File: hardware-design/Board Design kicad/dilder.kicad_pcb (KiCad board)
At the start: 4 copper layers, 45 x 80 mm, 27 parts, among them J1 USB-C, J2 BAT, J3 ePaper, Q1 FS8205A, SW1 5-Way, U1 ESP32-S3-N16R8, U2 TP4056, U3 DW01A, U4 AMS1117-3.3, U6 MPU-6050

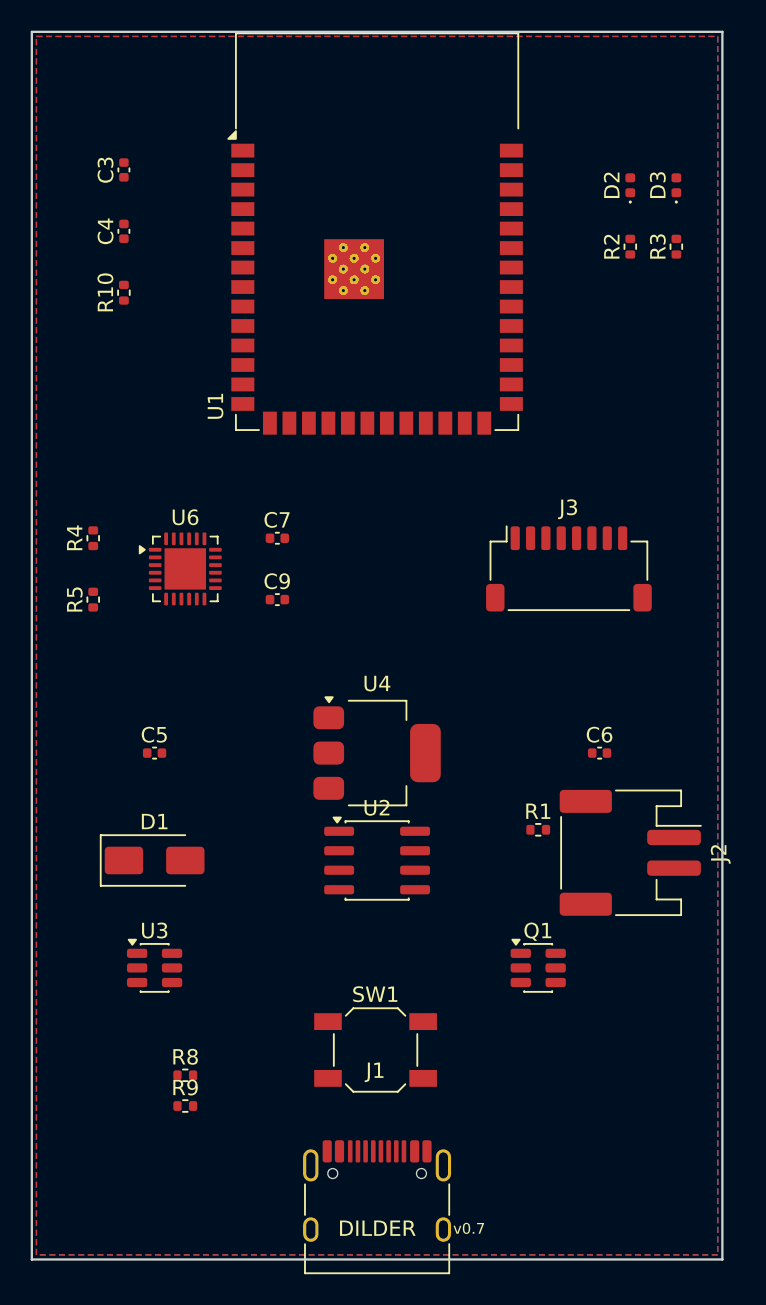
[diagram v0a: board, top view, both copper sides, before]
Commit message: Add v0.4 PCB routing, board design doc, update prompts, Prompt #155
Route the v0.4 board (30x70mm, 4-layer) with route_v04.py: B.Cu channels
for I2C/USB/joystick/ePaper, staggered L-routes for crossing-free SPI,
custom paths for EN/BOOT/battery protection, F.Cu power chain. Adds In1.Cu
GND plane and In2.Cu 3V3 plane with stitching vias. Board design doc
captures zones, BOM, GPIO map, routing strategy, and DRC status. Updates
prompts index with #154-155.

Co-Authored-By: Claude Opus 4.6 (1M context) <noreply@anthropic.com>
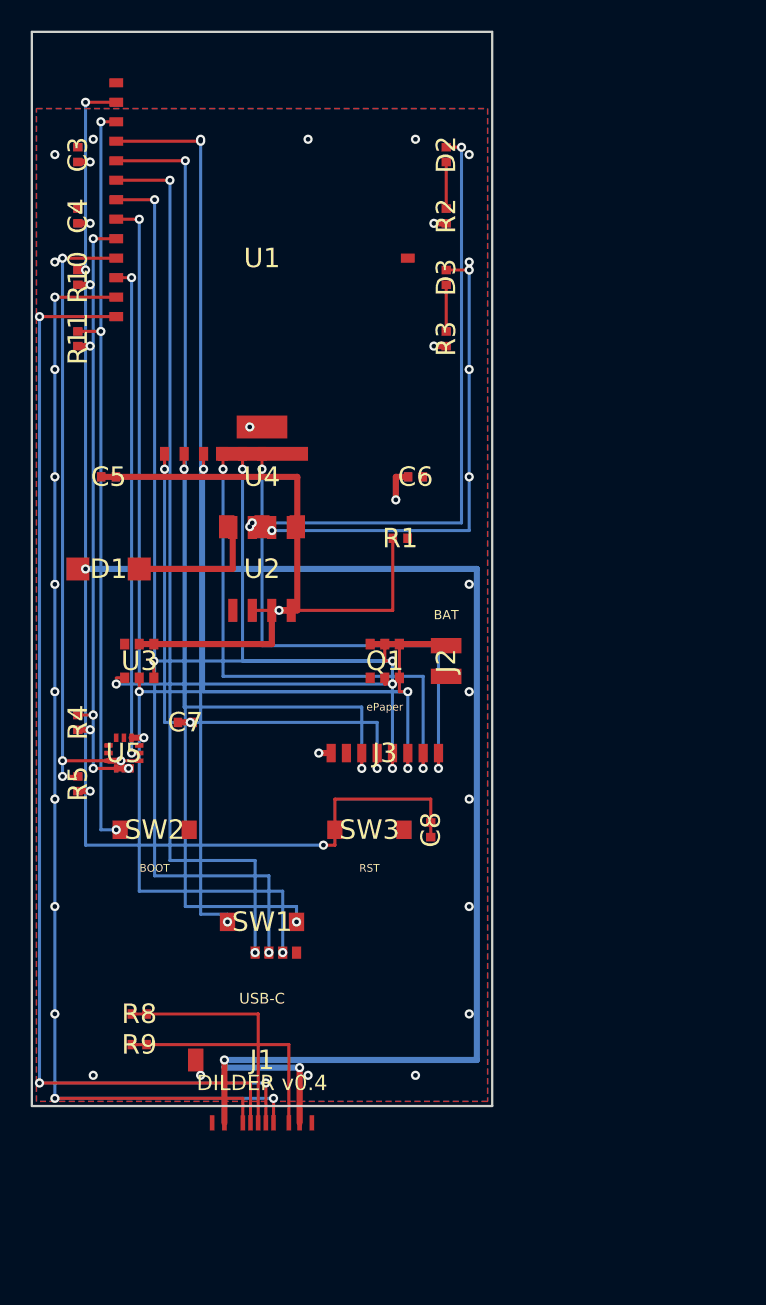
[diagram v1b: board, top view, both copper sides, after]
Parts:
- removed C9: 100nF, C_0402_1005Metric
- removed U6: MPU-6050, QFN-24-1EP_4x4mm_P0.5mm_EP2.7x2.7mm
- added C8: 100nF, , F.Cu at (126.0, 152.0)
- added R11: 10k, , F.Cu at (103.0, 120.0)
- added SW2: BOOT, , F.Cu at (108.0, 152.0)
- added SW3: RESET, , F.Cu at (122.0, 152.0)
- added U5: LIS2DH12TR, , F.Cu at (106.0, 147.0)
- C3, C4, C5, C6, C7: footprint C_0402_1005Metric -> (none)
- D1: footprint D_SMA -> (none)
- D2, D3: footprint LED_0402_1005Metric -> (none)
- J1: footprint USB_C_Receptacle_HRO_TYPE-C-31-M-12 -> (none)
- J2: footprint JST_PH_S2B-PH-SM4-TB_1x02-1MP_P2.00mm_Horizontal -> (none)
- J3: footprint JST_SH_SM08B-SRSS-TB_1x08-1MP_P1.00mm_Horizontal -> (none)
- Q1, U3: footprint SOT-23-6 -> (none)
- R1, R10, R2, R3, R4, R5, R8, R9: footprint R_0402_1005Metric -> (none)
- SW1: footprint SW_SPST_SKQG_WithStem -> (none)
- U1: footprint ESP32-S3-WROOM-1 -> (none)
- U2: footprint SOIC-8_3.9x4.9mm_P1.27mm -> (none)
- U4: footprint SOT-223-3_TabPin2 -> (none)
- moved Q1 22.4 mm to (123.0, 141.0)
- moved C6 21.6 mm to (125.0, 129.0)
- moved R1 21.0 mm to (124.0, 133.0)
- moved U2 20.4 mm to (115.0, 135.0)
- moved U3 20.0 mm to (107.0, 141.0)
- moved U4 19.5 mm to (115.0, 129.0)
- moved D1 19.2 mm to (105.0, 135.0)
- moved C5 18.2 mm to (105.0, 129.0)
- moved J2 17.3 mm to (127.0, 141.0)
- moved J3 17.0 mm to (123.0, 147.0)
- moved D3 16.2 mm to (127.0, 116.0)
- moved R3 16.2 mm to (127.0, 120.0)
- moved C7 13.4 mm to (110.0, 145.0)
- moved J1 12.5 mm to (115.0, 167.0)
- moved D2 12.2 mm to (127.0, 108.0)
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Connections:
- SW1 pad 1: GND -> JOY_UP
- SW1 pad 2: JOY_CENTER -> JOY_DOWN
- U1 pad 11: (no net) -> ACCEL_INT1
- U1 pad 27: (no net) -> BOOT
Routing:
- net USB_DP: track 0.00 -> 88.6 mm, vias 0 -> 3
- net VBUS: track 0.00 -> 87.5 mm, vias 0 -> 3
- net USB_DM: track 0.00 -> 85.9 mm, vias 0 -> 3
- net EN: track 0.00 -> 78.9 mm, vias 0 -> 3
- net JOY_DOWN: track 0.00 -> 61.3 mm, vias 0 -> 2
- net JOY_LEFT: track 0.00 -> 59.4 mm, vias 0 -> 2
- net JOY_RIGHT: track 0.00 -> 59.0 mm, vias 0 -> 2
- net JOY_CENTER: track 0.00 -> 58.6 mm, vias 0 -> 2
- net JOY_UP: track 0.00 -> 58.1 mm, vias 0 -> 2
- net BOOT: track 0.00 -> 50.1 mm, vias 0 -> 3
- net I2C_SCL: track 0.00 -> 43.3 mm, vias 0 -> 3
- net I2C_SDA: track 0.00 -> 39.5 mm, vias 0 -> 3
- net CHRG_OUT: track 0.00 -> 39.4 mm, vias 0 -> 2
- net EPD_CLK: track 0.00 -> 35.3 mm, vias 0 -> 2
- net EPD_DC: track 0.00 -> 34.8 mm, vias 0 -> 2
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- added copper zone on In2.Cu, net 3V3
- added copper zone on In1.Cu, net GND
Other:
- board size 45 x 80 mm -> 30 x 70 mm
- board text added: "BAT"
- board text added: "BOOT"
- board text added: "DILDER v0.4"
- board text added: "RST"
- board text added: "USB-C"
- board text added: "dilder.dev"
- board text added: "ePaper"
- board text added: "v0.4 2026"
- board text removed: "v0.7"

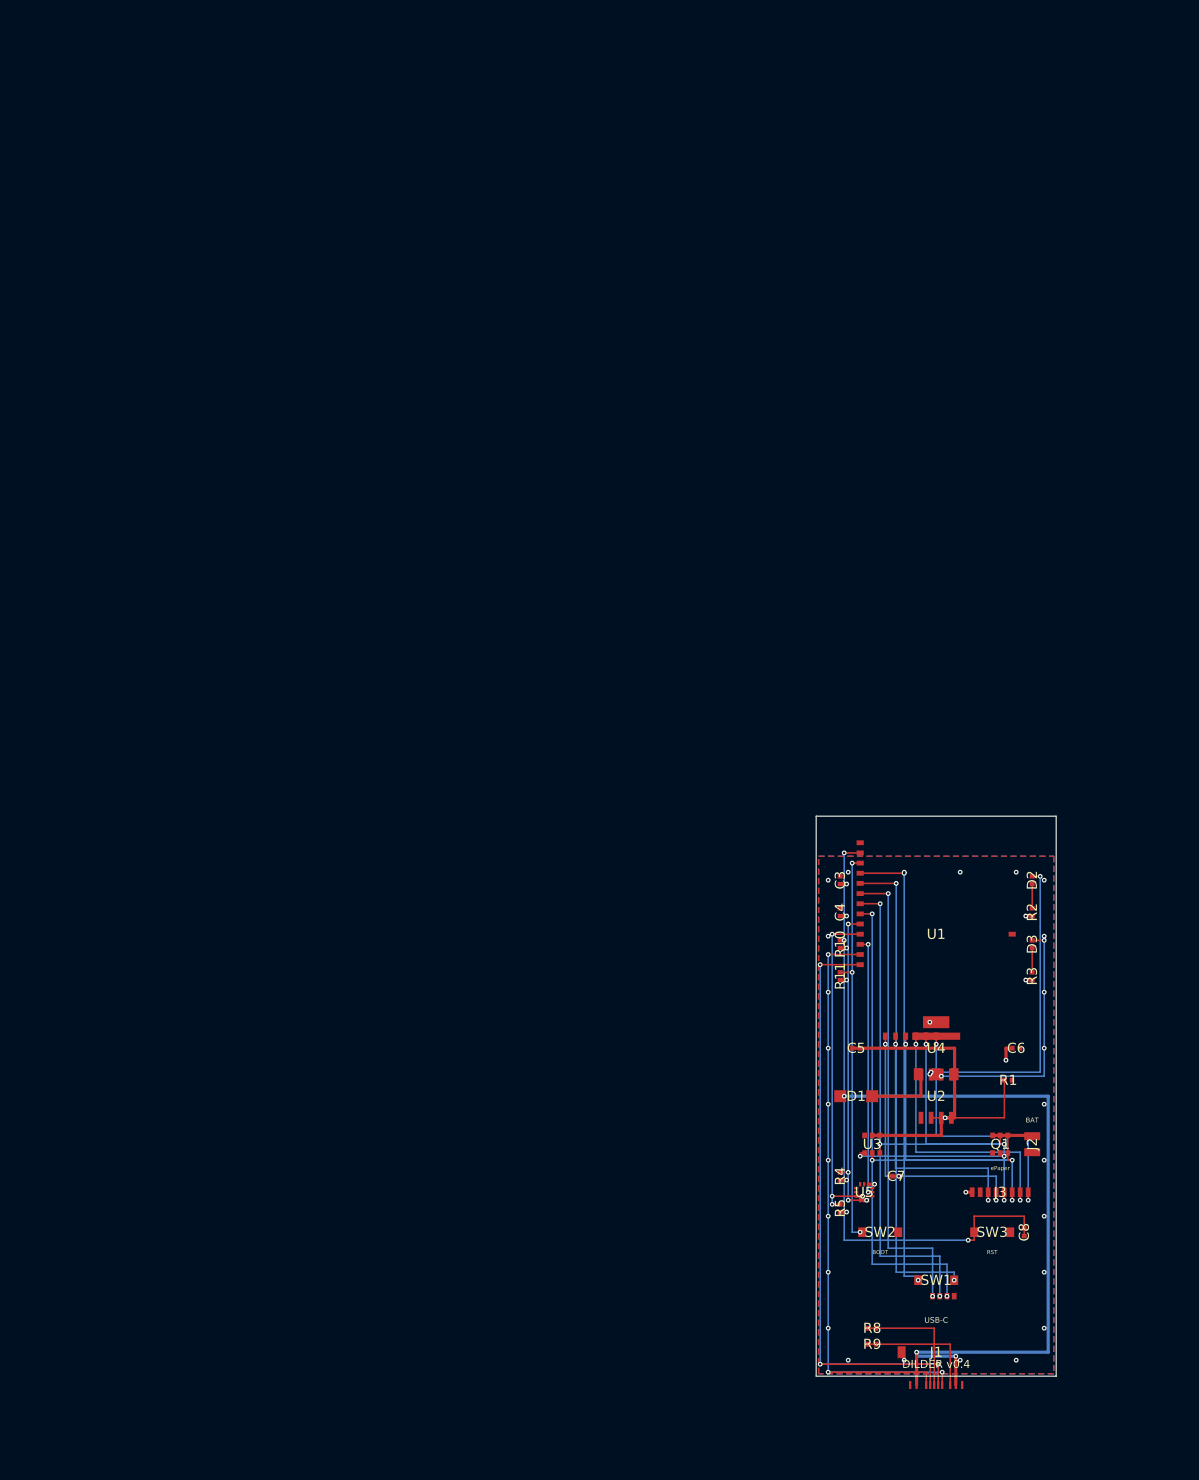
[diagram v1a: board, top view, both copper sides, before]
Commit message: Add user guide, asset system, feature menus, KiCad sensor updates, blog posts, Prompt #162
User guide (1,207 lines) covering all planned features as if implemented:
story, 16 emotions, stat system, 64 achievements, 6 evolutions, controls.
Feature systems doc (963 lines) with achievement registry, menu viewer
specs, toast notifications, decor browser, and full menu hierarchy.

Asset rendering pipeline: 52 Python modules generating 22 environments,
42 outfits, 29 decor props, 16 aura particle sets, and emotion previews.
Grid compilation images copied to website for blog showcases.

KiCad schematic + PCB updated with AHT20 and BH1750 sensors on shared
I2C bus. BOM, board design docs, wiring pinout updated accordingly.

New blog post on asset rendering system with image showcases.
User guide published to website docs. Prompts #161-#162 logged.

Co-Authored-By: Claude Opus 4.6 (1M context) <noreply@anthropic.com>
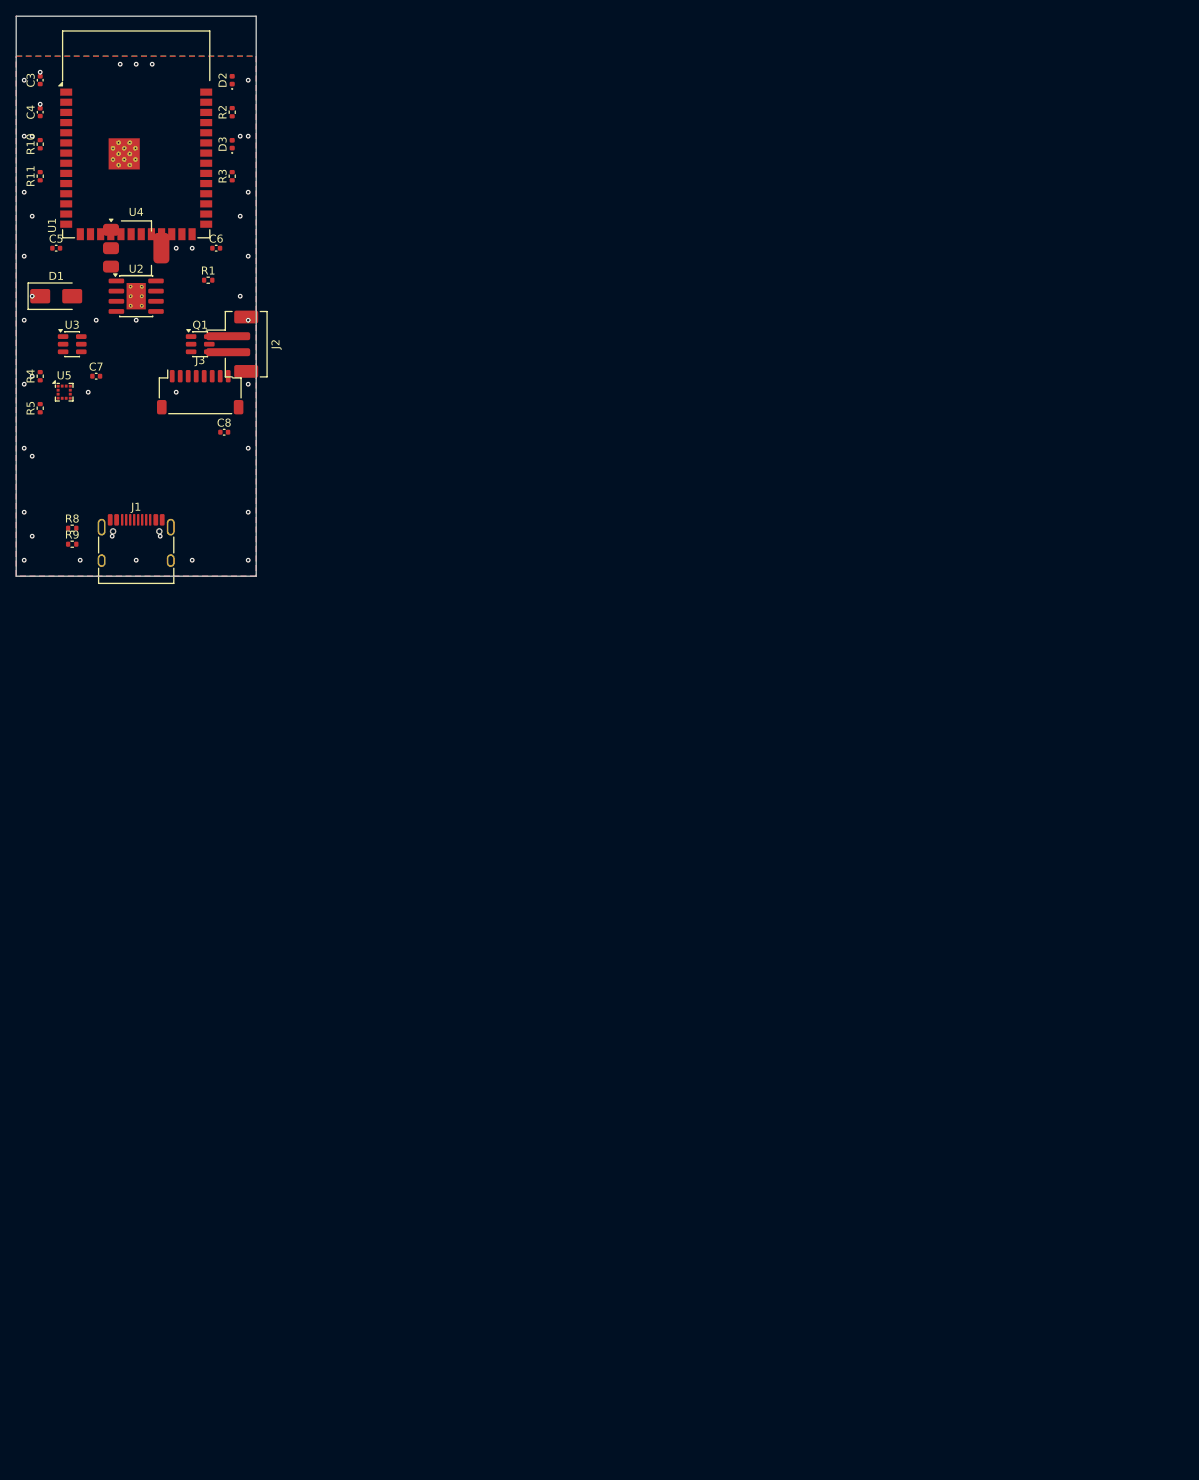
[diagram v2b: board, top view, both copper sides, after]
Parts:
- removed SW1: 5-Way, 
- removed SW2: BOOT, 
- removed SW3: RESET, 
- C3, C4, C5, C6, C7, C8: footprint (none) -> C_0402_1005Metric
- D1: footprint (none) -> D_SMA
- D2, D3: footprint (none) -> LED_0402_1005Metric
- J1: footprint (none) -> USB_C_Receptacle_HRO_TYPE-C-31-M-12
- J2: footprint (none) -> JST_PH_B2B-PH-SM4-TB_1x02-1MP_P2.00mm_Vertical
- J3: footprint (none) -> JST_SH_SM08B-SRSS-TB_1x08-1MP_P1.00mm_Horizontal
- Q1, U3: footprint (none) -> SOT-23-6
- R1, R10, R11, R2, R3, R4, R5, R8, R9: footprint (none) -> R_0402_1005Metric
- U1: value ESP32-S3-N16R8 -> ESP32-S3-WROOM-1-N16R8; footprint (none) -> ESP32-S3-WROOM-1
- U2: footprint (none) -> SOIC-8-1EP_3.9x4.9mm_P1.27mm_EP2.41x3.3mm_ThermalVias
- U4: footprint (none) -> SOT-223-3_TabPin2
- U5: footprint (none) -> LGA-12_2x2mm_P0.5mm
- moved C3 141.4 mm to (3.00, 8.00)
- moved C4 141.4 mm to (3.00, 12.0)
- moved C5 141.4 mm to (5.00, 29.0)
- moved C6 141.4 mm to (25.0, 29.0)
- moved C7 141.4 mm to (10.0, 45.0)
- moved C8 141.4 mm to (26.0, 52.0), turned to 0 degrees
- moved D1 141.4 mm to (5.00, 35.0)
- moved D2 141.4 mm to (27.0, 8.00)
- moved D3 141.4 mm to (27.0, 16.0)
- moved J1 141.4 mm to (15.0, 67.0)
- moved J2 141.4 mm to (27.0, 41.0)
- moved J3 141.4 mm to (23.0, 47.0)
- moved Q1 141.4 mm to (23.0, 41.0)
- moved R1 141.4 mm to (24.0, 33.0)
- moved R10 141.4 mm to (3.00, 16.0)
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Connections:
- net BOOT renamed /BOOT
- net CC1 renamed /CC1
- net CC2 renamed /CC2
- net EN renamed /EN
- net EPD_BUSY renamed /EPD_BUSY
- net EPD_CLK renamed /EPD_CLK
- net EPD_CS renamed /EPD_CS
- net EPD_DC renamed /EPD_DC
- net EPD_MOSI renamed /EPD_MOSI
- net EPD_RST renamed /EPD_RST
- net OC renamed /OC
- net OD renamed /OD
- C5 pad 1: VBAT -> /VBAT
- D1 pad 1: VBUS -> (no net)
- D1 pad 2: VBUS_CHG -> (no net)
- D2 pad 1: CHRG_LED -> (no net)
- D2 pad 2: CHRG_OUT -> (no net)
- D3 pad 1: STDBY_LED -> (no net)
- D3 pad 2: STDBY_OUT -> (no net)
- J1 pad A12: GND -> (no net)
- J1 pad A4: VBUS -> PWR_FLAG
- J1 pad A6: USB_DP -> /USB_DP
- J1 pad A7: USB_DM -> /USB_DM
- J1 pad B1: GND -> (no net)
- J1 pad B12: GND -> (no net)
- J1 pad B4: VBUS -> (no net)
- J1 pad B6: USB_DP -> (no net)
- J1 pad B7: USB_DM -> (no net)
- J2 pad 1: BAT_PLUS -> /VBAT
- J2 pad 2: GND -> /BAT_MINUS
- Q1 pad 1: GND -> /BAT_MINUS
- Q1 pad 3: CS_DRAIN -> /CS_DRAIN
- Q1 pad 4: CS_DRAIN -> /CS_DRAIN
- Q1 pad 6: BAT_PLUS -> GND
- R1 pad 1: PROG -> (no net)
- R2 pad 1: 3V3 -> (no net)
- R2 pad 2: CHRG_LED -> GND
- R3 pad 1: 3V3 -> (no net)
- R3 pad 2: STDBY_LED -> GND
- R4 pad 2: I2C_SDA -> /I2C_SDA
- R5 pad 2: I2C_SCL -> /I2C_SCL
- U1 pad 10: I2C_SCL -> /I2C_SCL
- U1 pad 11: ACCEL_INT1 -> /ACCEL_INT1
- U1 pad 13: USB_DM -> /USB_DM
- U1 pad 14: USB_DP -> /USB_DP
- U1 pad 31: GND -> (no net)
- U1 pad 32: GND -> (no net)
- U1 pad 4: JOY_UP -> /JOY_UP
- U1 pad 40: GND -> (no net)
- U1 pad 41: GND -> (no net)
- U1 pad 5: JOY_DOWN -> GND
- U1 pad 6: JOY_LEFT -> GND
- U1 pad 7: JOY_RIGHT -> GND
- U1 pad 8: JOY_CENTER -> GND
- U1 pad 9: I2C_SDA -> /I2C_SDA
- U2 pad 2: PROG -> (no net)
- U2 pad 3: VBAT -> GND
- U2 pad 4: 3V3 -> /VBUS_CHG
- U2 pad 5: GND -> /VBAT
- U2 pad 6: STDBY_OUT -> /STDBY_OUT
- U2 pad 7: CHRG_OUT -> /CHRG_OUT
- U2 pad 8: VBUS_CHG -> /VBUS_CHG
- U3 pad 2: CS_DRAIN -> /CS_DRAIN
- U3 pad 4: VBAT -> /VBAT
- U3 pad 5: VBAT -> /VBAT
- U3 pad 6: GND -> /CS_DRAIN
- U4 pad 3: VBAT -> /VBAT
- U5 pad 1: 3V3 -> /I2C_SCL
- U5 pad 10: 3V3 -> (no net)
- U5 pad 12: (no net) -> /ACCEL_INT1
- U5 pad 2: GND -> 3V3
- U5 pad 4: 3V3 -> /I2C_SDA
- U5 pad 5: GND -> (no net)
- U5 pad 6: I2C_SDA -> GND
- U5 pad 7: I2C_SCL -> (no net)
- U5 pad 8: ACCEL_INT1 -> (no net)
- U5 pad 9: (no net) -> 3V3
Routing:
- net USB_DP: track 88.6 -> 0.00 mm, vias 3 -> 0
- net VBUS: track 87.5 -> 0.00 mm, vias 3 -> 0
- net USB_DM: track 85.9 -> 0.00 mm, vias 3 -> 0
- net /EN: track 78.9 -> 0.00 mm, vias 3 -> 0
- net JOY_DOWN: track 61.3 -> 0.00 mm, vias 2 -> 0
- net JOY_LEFT: track 59.4 -> 0.00 mm, vias 2 -> 0
- net JOY_RIGHT: track 59.0 -> 0.00 mm, vias 2 -> 0
- net JOY_CENTER: track 58.6 -> 0.00 mm, vias 2 -> 0
- net JOY_UP: track 58.1 -> 0.00 mm, vias 2 -> 0
- net /BOOT: track 50.1 -> 0.00 mm, vias 3 -> 0
- net I2C_SCL: track 43.3 -> 0.00 mm, vias 3 -> 0
- net I2C_SDA: track 39.5 -> 0.00 mm, vias 3 -> 0
- net CHRG_OUT: track 39.4 -> 0.00 mm, vias 2 -> 0
- net /EPD_CLK: track 35.3 -> 0.00 mm, vias 2 -> 0
- net /EPD_DC: track 34.8 -> 0.00 mm, vias 2 -> 0
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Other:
- board text removed: "BAT"
- board text removed: "BOOT"
- board text removed: "DILDER"
- board text removed: "DILDER v0.4"
- board text removed: "RST"
- board text removed: "USB-C"
- board text removed: "dilder.dev"
- board text removed: "ePaper"
- board text removed: "v0.4 2026"
